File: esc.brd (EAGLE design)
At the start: 50.8 x 38.1 mm, 35 parts, among them U1 AON6558, U2 AON6558, U3 AON6558, U4 AON6558, U5 ATTINY20, U6 DRV8701

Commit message: Update to V2.1
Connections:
- net 5V: now also U$2.4
- net GND: no longer U$2.4
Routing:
- net 5V: track 62.2 -> 68.4 mm
- net GND: vias 159 -> 152
- added copper zone on layer 1, net 5V
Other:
- board text added: "Puma ESC v2.1"
- board text added: "Schatz"
- board text removed: "PUMA ESC"
- board text removed: "SCHATZ v2"
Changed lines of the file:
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@@
 <wire x1="1.27" y1="0" x2="1.27" y2="-38.1" width="0.3048" layer="20"/>
 <wire x1="1.27" y1="-38.1" x2="52.07" y2="-38.1" width="0.3048" layer="20"/>
-<text x="2.413" y="-3.175" size="1.778" layer="25">PUMA ESC</text>
-<text x="2.413" y="-5.334" size="1.778" layer="25">SCHATZ v2</text>
+<text x="2.413" y="-3.175" size="1.778" layer="25">Puma ESC v2.1</text>
+<text x="2.413" y="-5.334" size="1.778" layer="25">Schatz</text>
 <polygon width="0.0000125" layer="26">
 <vertex x="-8.9312375" y="-4.3688"/>
@@
 <contactref element="U6" pad="21"/>
 <contactref element="U6" pad="20"/>
-<polygon width="0.9144" layer="1" thermals="no">
-<vertex x="24.892" y="-24.384"/>
-<vertex x="28.448" y="-24.384"/>
-<vertex x="28.448" y="-26.416"/>
-<vertex x="24.892" y="-26.416"/>
-</polygon>
-<contactref element="U$2" pad="4"/>
 <polygon width="0.3048" layer="1" isolate="0.3048" rank="2">
 <vertex x="1.27" y="0"/>
@@
 <via x="30.48" y="-22.479" extent="1-16" drill="0.35"/>
 <via x="31.242" y="-23.241" extent="1-16" drill="0.35"/>
-<via x="29.4005" y="-24.892" extent="1-16" drill="0.35"/>
 <via x="19.431" y="-12.319" extent="1-16" drill="0.35"/>
 <via x="6.096" y="-26.543" extent="1-16" drill="0.35"/>
@@
 <via x="13.8684" y="-26.797" extent="1-16" drill="0.35"/>
 <via x="18.3642" y="-28.6766" extent="1-16" drill="0.35"/>
-<via x="22.5552" y="-29.6164" extent="1-16" drill="0.35"/>
-<via x="24.384" y="-29.2862" extent="1-16" drill="0.35"/>
-<via x="27.3304" y="-29.3624" extent="1-16" drill="0.35"/>
 <via x="30.988" y="-28.2448" extent="1-16" drill="0.35"/>
 <via x="31.0134" y="-24.7142" extent="1-16" drill="0.35"/>
-<via x="29.7434" y="-26.543" extent="1-16" drill="0.35"/>
-<via x="28.0924" y="-27.432" extent="1-16" drill="0.35"/>
-<via x="24.4602" y="-27.3304" extent="1-16" drill="0.35"/>
-<via x="22.3774" y="-27.2542" extent="1-16" drill="0.35"/>
+<via x="31.4452" y="-26.1874" extent="1-16" drill="0.35"/>
 <via x="20.0152" y="-27.0002" extent="1-16" drill="0.35"/>
-<via x="24.1681" y="-25.2476" extent="1-16" drill="0.35"/>
 <via x="30.8356" y="-16.6624" extent="1-16" drill="0.35"/>
 <via x="30.8356" y="-18.5166" extent="1-16" drill="0.35"/>
-<via x="22.225" y="-25.0952" extent="1-16" drill="0.35"/>
 <via x="17.5006" y="-26.4922" extent="1-16" drill="0.35"/>
 <via x="18.161" y="-24.6126" extent="1-16" drill="0.35"/>
@@
 <via x="13.843" y="-19.177" extent="1-16" drill="0.35"/>
 <via x="13.0175" y="-21.209" extent="1-16" drill="0.35"/>
+<via x="27.178" y="-23.241" extent="1-16" drill="0.35"/>
+<via x="30.2895" y="-30.607" extent="1-16" drill="0.35"/>
 </signal>
 <signal name="SH1" class="1">
@@
 <wire x1="26.67" y1="-34.3925" x2="26.67" y2="-31.5468" width="0.6096" layer="1"/>
 <wire x1="26.6455" y1="-34.417" x2="24.2635" y2="-34.417" width="0.6096" layer="1"/>
+<contactref element="U$2" pad="4"/>
+<wire x1="26.67" y1="-31.5468" x2="26.67" y2="-25.349" width="0.6096" layer="1"/>
+<polygon width="0.6096" layer="1" thermals="no">
+<vertex x="23.368" y="-24.3205"/>
+<vertex x="29.718" y="-24.3205"/>
+<vertex x="29.718" y="-29.7815"/>
+<vertex x="23.495" y="-29.7815"/>
+<vertex x="23.3045" y="-29.7815"/>
+<vertex x="23.3045" y="-29.718"/>
+<vertex x="23.3045" y="-24.3205"/>
+</polygon>
 </signal>
 <signal name="TPICLK">

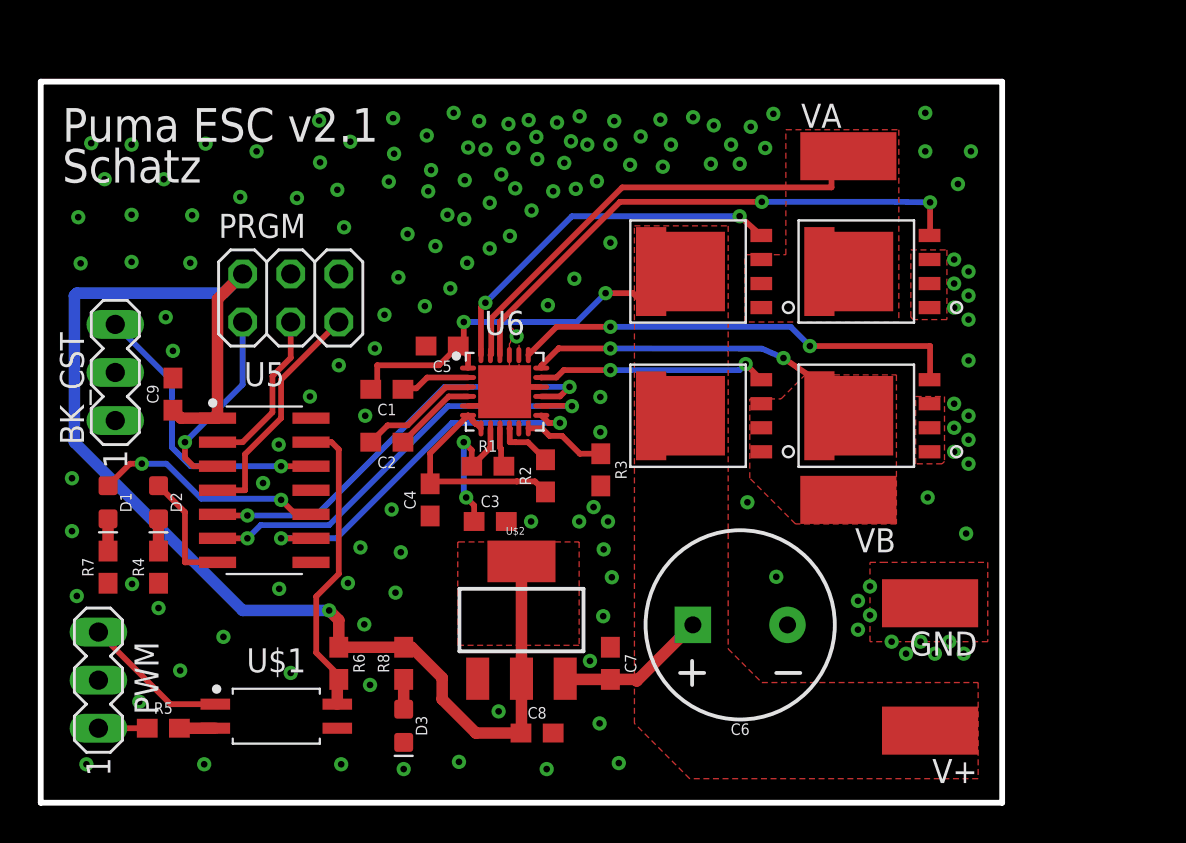
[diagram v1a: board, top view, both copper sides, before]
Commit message: Update to board v3
New power connectors and compactify layout
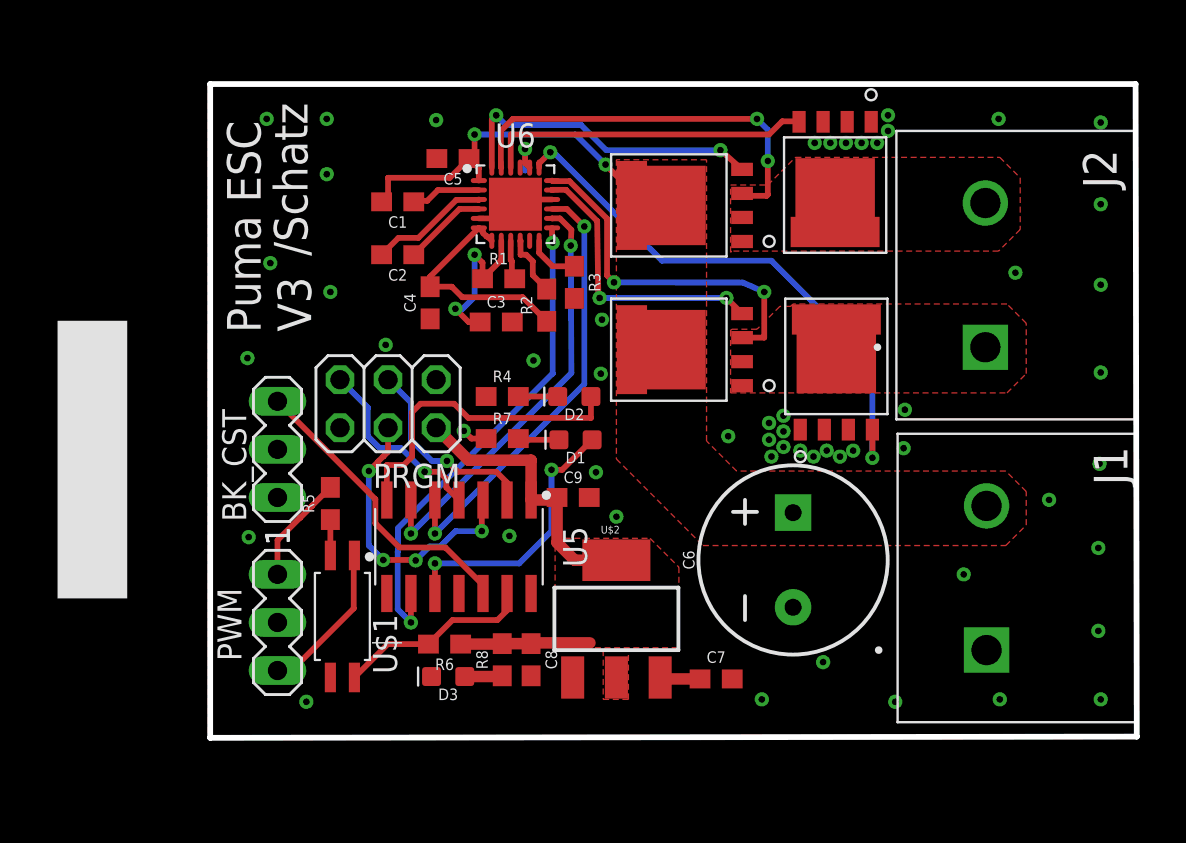
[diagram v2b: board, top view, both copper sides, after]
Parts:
- removed GND, V+, VA, VB: (no value), wirepad:SMD2,54-5,08
- added J1, J2: TB005-762-02BE, TB005-762-02BE:CUI_TB005-762-02BE
- moved D1 24.9 mm to (29.5, -18.9), turned to 180 degrees
- moved D2 22.7 mm to (29.5, -16.6), turned to 180 degrees
- moved R7 21.9 mm to (25.7, -18.9), turned to 0 degrees
- moved C9 21.8 mm to (29.4, -22.0), turned to 0 degrees
- moved R4 20.3 mm to (25.7, -16.6), turned to 0 degrees
- moved R5 14.8 mm to (16.6, -22.3), turned to 270 degrees
- moved U5 10.7 mm to (23.4, -24.6), turned to 270 degrees
- moved C3 10.5 mm to (25.3, -12.7)
- moved C4 10.4 mm to (21.8, -11.7)
- moved R3 10.0 mm to (29.5, -10.6)
- moved PWM 9.94 mm to (13.8, -28.6), turned to 270 degrees
- moved C1 9.92 mm to (20.1, -6.35)
- moved C2 9.92 mm to (20.1, -9.14)
- moved C5 9.92 mm to (23.1, -4.06)
- moved R1 9.92 mm to (25.5, -10.4)
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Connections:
- net GND: now also J1.1; no longer GND.1
- net SH1: now also J2.1; no longer VB.1
- net SH2: now also J2.2; no longer VA.1
- net TPIDATA: now also PRGM.4; no longer PRGM.1
- net V_BATT: now also J1.2; no longer V+.1
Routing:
- net 5V: track 68.4 -> 23.4 mm, vias 1 -> 0
- net GL2: track 28.9 -> 17.3 mm, vias 2 -> 0
- net N$4: track 6.35 -> 16.8 mm
- net V_BATT: track 27.5 -> 20.6 mm
- net NSLEEP: track 20.0 -> 26.1 mm
- net SIG_IN: track 16.1 -> 10.4 mm
- net GL1: track 24.1 -> 29.2 mm
- net TPIDATA: track 10.3 -> 15.3 mm, vias 1 -> 4
- net SH1: track 15.5 -> 19.1 mm
- net GND: track 4.28 -> 7.86 mm, vias 152 -> 55
- net SH2: track 24.8 -> 21.4 mm, vias 0 -> 2
- net IN_GND: track 2.58 -> 5.76 mm
- net GH1: track 12.3 -> 15.0 mm
- net GH2: track 19.7 -> 17.0 mm
- net /RST: track 12.5 -> 10.1 mm, vias 0 -> 1
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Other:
- board size 50.8 x 38.1 mm -> 49 x 34.5 mm
- board text added: "/Schatz"
- board text added: "Puma ESC"
- board text added: "V3"
- board text removed: "Puma ESC v2.1"
- board text removed: "Schatz"

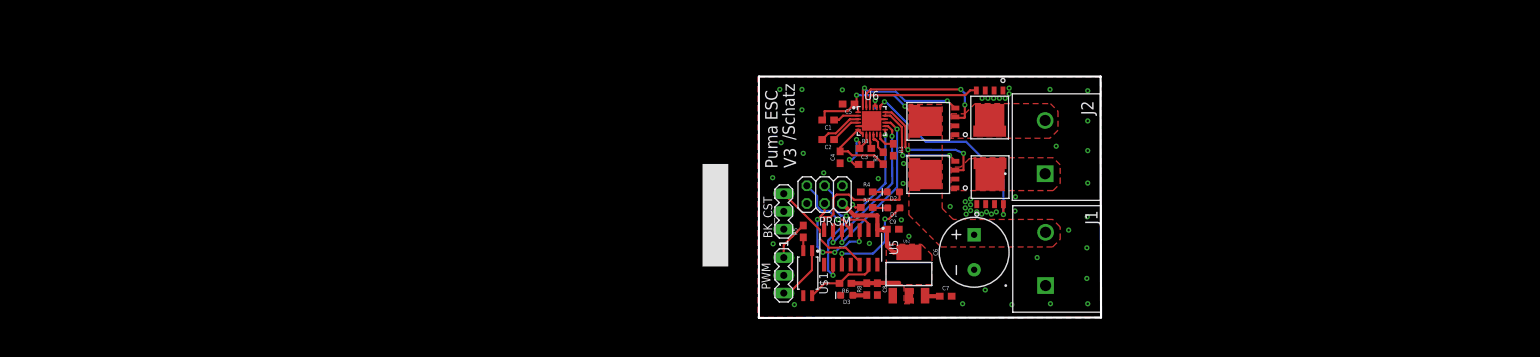
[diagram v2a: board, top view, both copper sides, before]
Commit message: Add current sense features
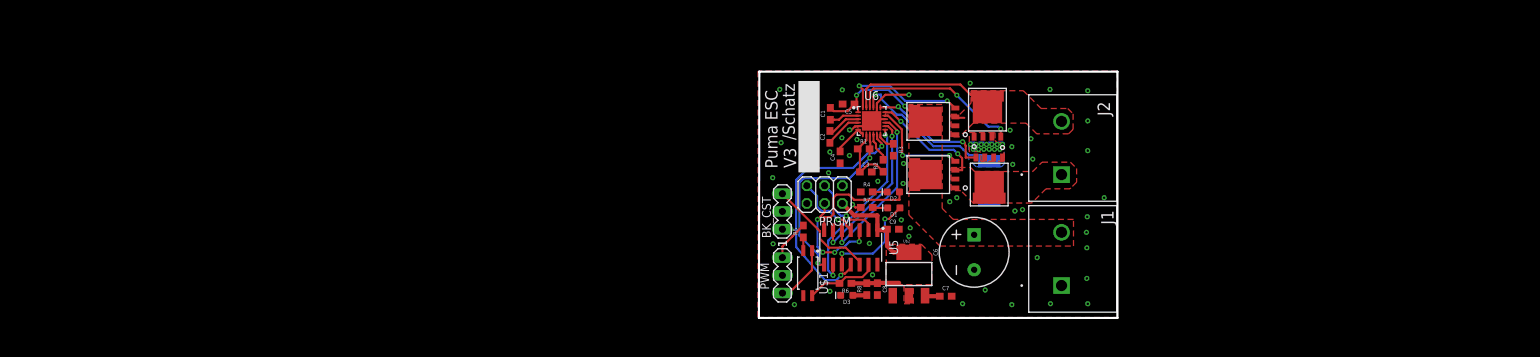
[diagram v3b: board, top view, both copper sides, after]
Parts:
- added R9: 12m, rcl:R2512
- moved J2 2.35 mm to (53.5, -14.2)
- moved J1 2.29 mm to (53.5, -30.0)
- moved C3 1.10 mm to (25.5, -13.8)
- moved R2 1.08 mm to (28.0, -12.9)
- moved C1 0.94 mm to (20.4, -5.46), turned to 90 degrees
- moved U2 0.65 mm to (42.9, -5.71), turned to 90 degrees
- moved U3 0.65 mm to (43.2, -14.7), turned to 270 degrees
- moved C2 0.46 mm to (20.4, -8.76), turned to 90 degrees
- moved R1 0.26 mm to (25.2, -10.5)
- moved BK_CST 0.19 mm to (13.6, -19.4)
- moved PWM 0.19 mm to (13.6, -28.6)
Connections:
- net N$11 renamed SNSOUT
- removed net N$10: R1.2, U6.9
- new net N$14: R9.1, U2.1, U2.2, U2.3, U3.1, U3.2, U3.3, U6.21
- new net NFAULT: R1.2, U5.8, U6.9
- new net SO: U5.11, U6.11
- net GND: now also R9.2; no longer U2.1, U2.2, U2.3, U3.1, U3.2, U3.3, U6.21
- net N$5: now also R2.1
- net N$7: no longer R2.1
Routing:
- net SO: track 0.00 -> 37.0 mm, vias 0 -> 2
- net NFAULT: track 0.00 -> 28.6 mm, vias 0 -> 2
- net N$14: track 0.00 -> 22.5 mm, vias 0 -> 14
- net GL1: track 29.2 -> 17.9 mm
- net GL2: track 17.3 -> 24.6 mm, vias 0 -> 2
- net N$7: track 12.1 -> 5.17 mm
- net GND: track 7.86 -> 14.6 mm, vias 55 -> 50
- net SH1: track 19.1 -> 16.5 mm
- net N$10: track 2.09 -> 0.00 mm
- net V_BATT: track 20.6 -> 19.2 mm
- net GH2: track 17.0 -> 18.3 mm
- net N$2: track 6.36 -> 5.07 mm
- net N$5: track 8.96 -> 10.2 mm, vias 2 -> 0
- net SH2: track 21.4 -> 20.3 mm, vias 2 -> 0
- net SNSOUT: track 3.32 -> 4.22 mm
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- added copper zone on layer 1, net N$14
- added copper zone on layer 16, net N$14
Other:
- board size 49 x 34.5 mm -> 51.3 x 35.2 mm

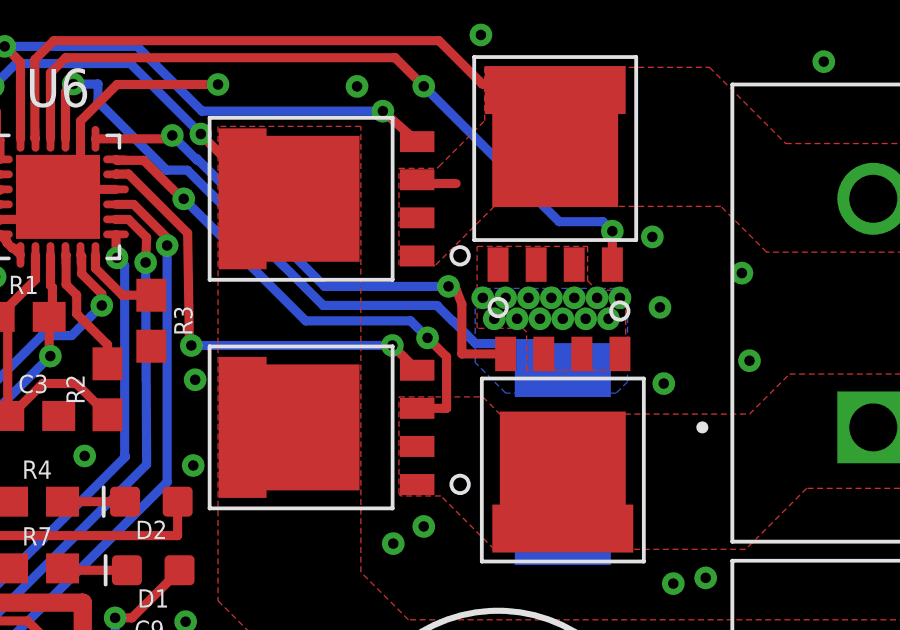
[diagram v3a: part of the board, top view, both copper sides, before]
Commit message: Minor via placement changes
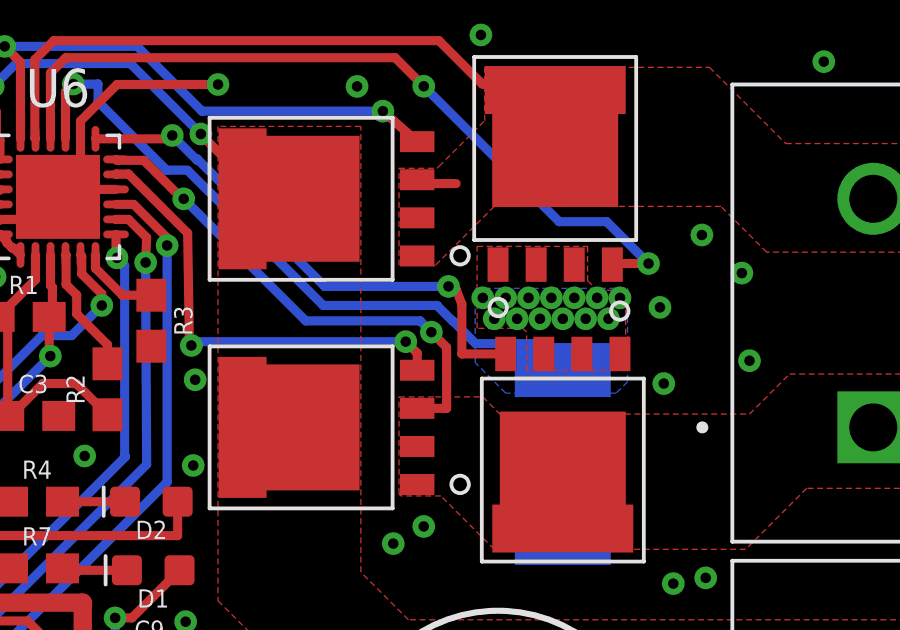
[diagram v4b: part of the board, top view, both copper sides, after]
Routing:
- net GL2: track 24.6 -> 26.4 mm
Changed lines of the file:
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@@
 <wire x1="24.257" y1="-24.3205" x2="24.257" y2="-24.892" width="0.3048" layer="42"/>
 <wire x1="32.8295" y1="-32.512" x2="33.02" y2="-32.512" width="0.3048" layer="41"/>
+<wire x1="45.593" y1="-7.239" x2="45.593" y2="-8.0645" width="0.3048" layer="41"/>
 </plain>
 <attributes>
@@
 <wire x1="27.1025" y1="-4.5424" x2="27.1025" y2="-3.949" width="0.3048" layer="1"/>
 <wire x1="27.1025" y1="-3.949" x2="28.321" y2="-2.7305" width="0.3048" layer="1"/>
-<via x="46.1645" y="-7.8105" extent="1-16" drill="0.35"/>
+<via x="47.8155" y="-7.747" extent="1-16" drill="0.35"/>
 <via x="46.5455" y="-12.7" extent="1-16" drill="0.35"/>
 <via x="46.4185" y="-10.16" extent="1-16" drill="0.35"/>
@@
 <contactref element="U3" pad="SIDEPAD2"/>
 <wire x1="34.6122875" y1="-10.61121875" x2="30.5431625" y2="-6.54209375" width="0.3048" layer="16"/>
-<wire x1="38.106896875" y1="-10.611396875" x2="34.6122875" y2="-10.61121875" width="0.3048" layer="16"/>
-<wire x1="38.106896875" y1="-10.611396875" x2="38.6715" y2="-11.176" width="0.3048" layer="16"/>
-<via x="38.6715" y="-11.176" extent="1-16" drill="0.35"/>
+<wire x1="38.4244125" y1="-10.6114125" x2="34.6122875" y2="-10.61121875" width="0.3048" layer="16"/>
+<wire x1="38.4244125" y1="-10.6114125" x2="38.7985" y2="-10.9855" width="0.3048" layer="16"/>
+<via x="38.7985" y="-10.9855" extent="1-16" drill="0.35"/>
 <contactref element="J2" pad="1"/>
 <wire x1="39.3065" y1="-13.5255" x2="38.326" y2="-13.5255" width="0.3048" layer="1"/>
@@
 <vertex x="37.719" y="-16.383"/>
 </polygon>
-<wire x1="38.6715" y1="-11.176" x2="39.3065" y2="-11.811" width="0.3048" layer="1"/>
-<wire x1="39.3065" y1="-11.811" x2="39.3065" y2="-13.5255" width="0.3048" layer="1"/>
+<wire x1="38.7985" y1="-10.9855" x2="39.3065" y2="-11.4935" width="0.3048" layer="1"/>
+<wire x1="39.3065" y1="-11.4935" x2="39.3065" y2="-13.5255" width="0.3048" layer="1"/>
 </signal>
 <signal name="SH2" class="1" airwireshidden="yes">
@@
 <wire x1="26.1025" y1="-4.5424" x2="26.0985" y2="-2.3495" width="0.3048" layer="1"/>
 <wire x1="26.0985" y1="-2.3495" x2="26.6105" y2="-1.8375" width="0.3048" layer="1"/>
-<wire x1="44.831" y1="-7.62" x2="44.831" y2="-8.735" width="0.3048" layer="1"/>
+<wire x1="46.0375" y1="-8.6995" x2="44.8665" y2="-8.6995" width="0.3048" layer="1"/>
+<wire x1="44.8665" y1="-8.6995" x2="44.831" y2="-8.735" width="0.3048" layer="1"/>
 <wire x1="37.592" y1="-1.8375" x2="26.6105" y2="-1.8375" width="0.3048" layer="1"/>
 <wire x1="37.592" y1="-1.8375" x2="38.5445" y2="-2.79" width="0.3048" layer="1"/>
 <via x="38.5445" y="-2.79" extent="1-16" drill="0.35"/>
-<wire x1="44.5135" y1="-7.3025" x2="44.831" y2="-7.62" width="0.3048" layer="16"/>
-<wire x1="44.5135" y1="-7.3025" x2="43.057" y2="-7.3025" width="0.3048" layer="16"/>
-<via x="44.831" y="-7.62" extent="1-16" drill="0.35"/>
+<wire x1="44.6405" y1="-7.3025" x2="46.0375" y2="-8.6995" width="0.3048" layer="16"/>
+<wire x1="44.6405" y1="-7.3025" x2="43.057" y2="-7.3025" width="0.3048" layer="16"/>
+<via x="46.0375" y="-8.6995" extent="1-16" drill="0.35"/>
 <wire x1="38.5445" y1="-2.79" x2="43.057" y2="-7.3025" width="0.3048" layer="16"/>
 </signal>
@@
 <contactref element="U4" pad="4"/>
 <wire x1="28.2874" y1="-5.7273" x2="28.2871" y2="-5.727" width="0.3048" layer="1"/>
-<wire x1="37.5005" y1="-11.43" x2="30.7975" y2="-11.43" width="0.3048" layer="16"/>
-<via x="37.5005" y="-11.43" extent="1-16" drill="0.35"/>
-<wire x1="37.5005" y1="-11.43" x2="38.326" y2="-12.2555" width="0.3048" layer="1"/>
+<wire x1="37.945" y1="-11.303" x2="30.9245" y2="-11.303" width="0.3048" layer="16"/>
+<wire x1="30.9245" y1="-11.303" x2="30.7975" y2="-11.43" width="0.3048" layer="16"/>
+<via x="37.945" y="-11.303" extent="1-16" drill="0.35"/>
+<wire x1="38.326" y1="-11.684" x2="37.945" y2="-11.303" width="0.3048" layer="1"/>
+<wire x1="38.326" y1="-11.684" x2="38.326" y2="-12.2555" width="0.3048" layer="1"/>
 <via x="30.7975" y="-11.43" extent="1-16" drill="0.35"/>
 <wire x1="30.7975" y1="-11.43" x2="30.732975" y2="-11.365475" width="0.3048" layer="1"/>
